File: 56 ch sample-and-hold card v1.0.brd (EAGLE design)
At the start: 170.8 x 36.2 mm, 124 parts, among them IC1 4051D, IC10 TL074JT, IC11 4051D, IC12 TL074JT, IC13 TL074JT, IC14 4051D, IC15 TL074JT, IC16 TL074JT, IC17 4051D, IC18 TL074JT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

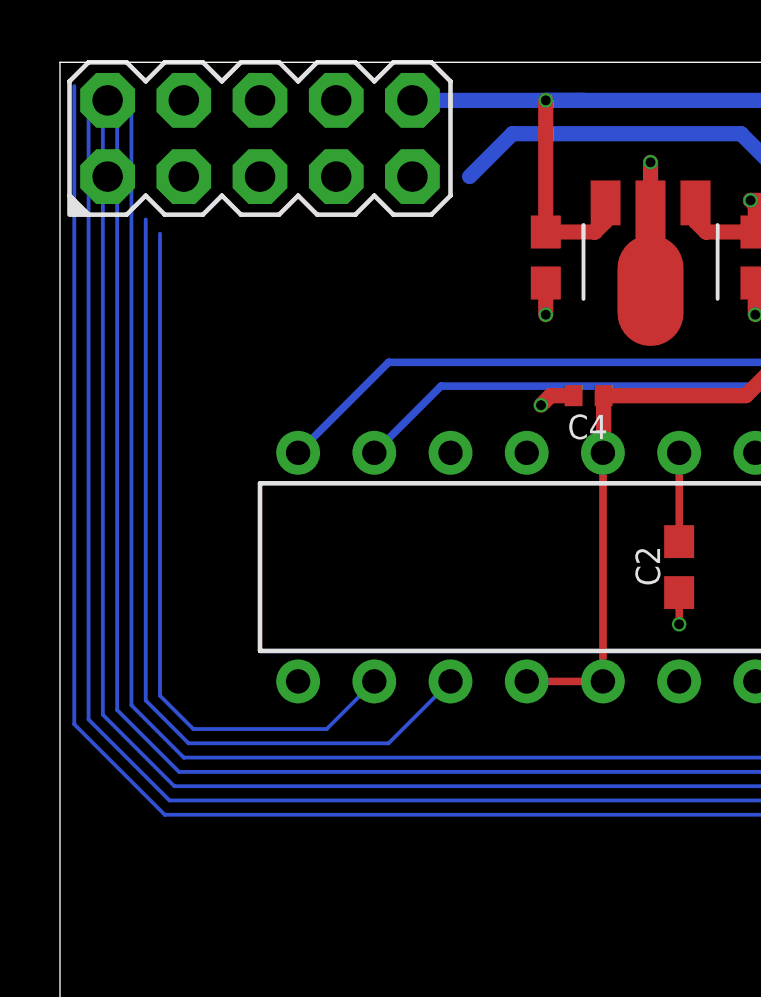
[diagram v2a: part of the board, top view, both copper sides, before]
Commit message: All routed, nothing tested
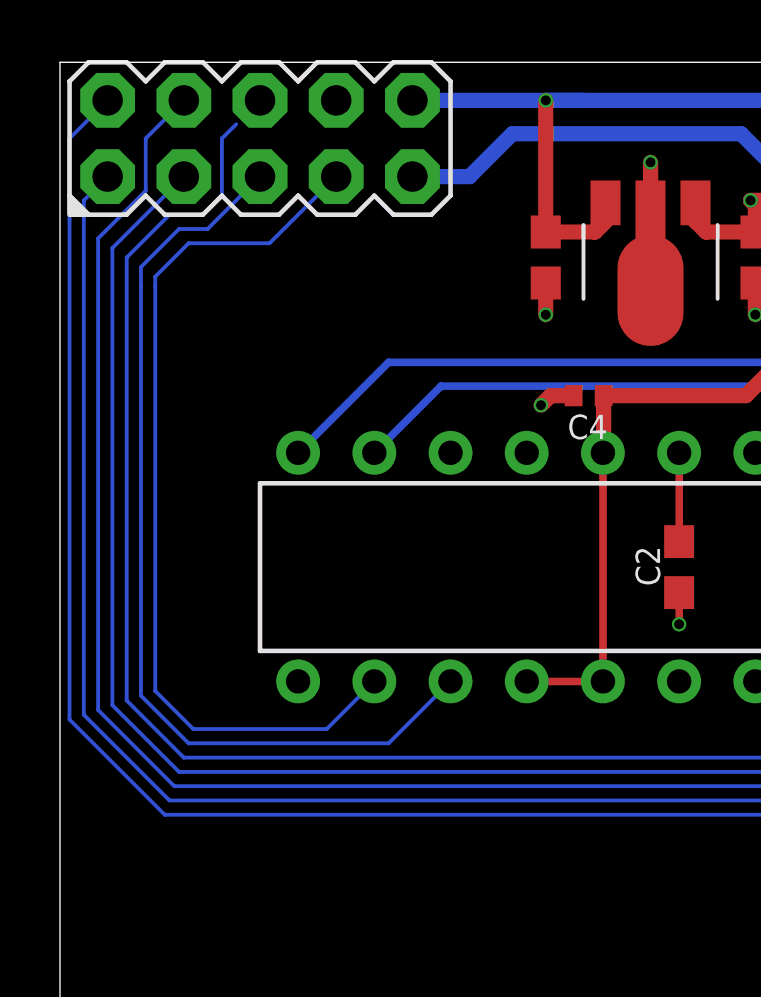
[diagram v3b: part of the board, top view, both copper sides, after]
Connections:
- new net GND: X1.8
- net +12V: now also X1.10
- net -12V: now also X1.9
- net A0: now also X1.2
- net A1: now also X1.1
- net A2: now also X1.4
- net INH_1: now also X1.3
- net INH_2: now also X1.6
- net SCK: now also X1.7
- net SDA: now also X1.5
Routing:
- net SCK: track 23.7 -> 29.7 mm
- net SDA: track 27.6 -> 31.3 mm
- net A1: track 202.0 -> 199.5 mm
- net -12V: track 191.3 -> 193.2 mm
- net INH_1: track 212.7 -> 210.9 mm
- net INH_2: track 177.0 -> 178.1 mm
- net +12V: track 196.6 -> 197.5 mm
- net A2: track 197.7 -> 198.6 mm
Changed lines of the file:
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@@
 <wire x1="23.495" y1="34.925" x2="17.4625" y2="34.925" width="0.508" layer="16"/>
 <wire x1="17.4625" y1="34.925" x2="16.1925" y2="34.925" width="0.508" layer="16"/>
-<wire x1="16.1925" y1="34.925" x2="12.7" y2="34.925" width="0.508" layer="16"/>
 <wire x1="16.1925" y1="30.53625" x2="17.83625" y2="30.53625" width="0.508" layer="1"/>
 <wire x1="18.186" y1="30.886" x2="18.186" y2="31.5085" width="0.508" layer="1"/>
@@
 <wire x1="77.94625" y1="29.36875" x2="67.78625" y2="29.36875" width="0.508" layer="16"/>
 <wire x1="57.62625" y1="29.36875" x2="47.46625" y2="29.36875" width="0.508" layer="16"/>
+<contactref element="X1" pad="10"/>
+<wire x1="16.1925" y1="34.925" x2="11.7475" y2="34.925" width="0.508" layer="16"/>
 </signal>
 <signal name="-12V">
@@
 <wire x1="59.69" y1="28.2575" x2="70.00875" y2="28.2575" width="0.508" layer="16"/>
 <wire x1="39.37" y1="28.2575" x2="49.68875" y2="28.2575" width="0.508" layer="16"/>
+<contactref element="X1" pad="9"/>
+<wire x1="13.6525" y1="32.385" x2="11.7475" y2="32.385" width="0.508" layer="16"/>
 </signal>
 <signal name="OUT_7">
@@
 <wire x1="36.5125" y1="11.1125" x2="28.2575" y2="11.1125" width="0.127" layer="16"/>
 <wire x1="117.7925" y1="14.7066" x2="117.7925" y2="11.1125" width="0.127" layer="1"/>
-<wire x1="3.4925" y1="11.1125" x2="0.47625" y2="14.12875" width="0.127" layer="16"/>
-<wire x1="0.47625" y1="14.12875" x2="0.47625" y2="35.40125" width="0.127" layer="16"/>
+<wire x1="3.4925" y1="11.1125" x2="0.3175" y2="14.2875" width="0.127" layer="16"/>
 <wire x1="28.2575" y1="11.1125" x2="3.4925" y2="11.1125" width="0.127" layer="16"/>
+<wire x1="0.3175" y1="30.95625" x2="0.3175" y2="33.655" width="0.127" layer="16"/>
+<wire x1="0.3175" y1="14.2875" x2="0.3175" y2="30.95625" width="0.127" layer="16"/>
+<contactref element="X1" pad="2"/>
+<wire x1="0.3175" y1="33.655" x2="1.5875" y2="34.925" width="0.127" layer="16"/>
 </signal>
 <signal name="A1">
@@
 <wire x1="35.2425" y1="11.58875" x2="28.09875" y2="11.58875" width="0.127" layer="16"/>
 <wire x1="116.5225" y1="14.7066" x2="116.5225" y2="11.58875" width="0.127" layer="1"/>
-<wire x1="3.65125" y1="11.58875" x2="0.9525" y2="14.2875" width="0.127" layer="16"/>
+<wire x1="3.65125" y1="11.58875" x2="0.79375" y2="14.44625" width="0.127" layer="16"/>
 <wire x1="28.09875" y1="11.58875" x2="3.65125" y2="11.58875" width="0.127" layer="16"/>
-<wire x1="0.9525" y1="14.2875" x2="0.9525" y2="35.2425" width="0.127" layer="16"/>
+<wire x1="0.79375" y1="31.59125" x2="0.79375" y2="14.44625" width="0.127" layer="16"/>
+<contactref element="X1" pad="1"/>
+<wire x1="1.5875" y1="32.385" x2="0.79375" y2="31.59125" width="0.127" layer="16"/>
 </signal>
 <signal name="A2">
@@
 <wire x1="33.9725" y1="12.065" x2="27.94" y2="12.065" width="0.127" layer="16"/>
 <wire x1="115.2525" y1="14.7066" x2="115.2525" y2="13.17625" width="0.127" layer="1"/>
-<wire x1="3.81" y1="12.065" x2="1.42875" y2="14.44625" width="0.127" layer="16"/>
-<wire x1="1.42875" y1="14.44625" x2="1.42875" y2="35.2425" width="0.127" layer="16"/>
+<wire x1="3.81" y1="12.065" x2="1.27" y2="14.605" width="0.127" layer="16"/>
 <wire x1="27.94" y1="12.065" x2="3.81" y2="12.065" width="0.127" layer="16"/>
+<wire x1="1.27" y1="14.605" x2="1.27" y2="30.32125" width="0.127" layer="16"/>
+<wire x1="1.27" y1="30.32125" x2="2.8575" y2="31.90875" width="0.127" layer="16"/>
+<wire x1="2.8575" y1="31.90875" x2="2.8575" y2="33.655" width="0.127" layer="16"/>
+<contactref element="X1" pad="4"/>
+<wire x1="2.8575" y1="33.655" x2="4.1275" y2="34.925" width="0.127" layer="16"/>
 </signal>
 <signal name="INH_1">
@@
 <wire x1="114.45875" y1="12.54125" x2="113.9825" y2="12.54125" width="0.127" layer="16"/>
 <wire x1="32.86125" y1="12.54125" x2="27.78125" y2="12.54125" width="0.127" layer="16"/>
-<wire x1="3.96875" y1="12.54125" x2="1.905" y2="14.605" width="0.127" layer="16"/>
-<wire x1="1.905" y1="14.605" x2="1.905" y2="35.2425" width="0.127" layer="16"/>
+<wire x1="3.96875" y1="12.54125" x2="1.74625" y2="14.76375" width="0.127" layer="16"/>
+<wire x1="1.74625" y1="14.76375" x2="1.74625" y2="30.00375" width="0.127" layer="16"/>
 <wire x1="27.78125" y1="12.54125" x2="3.96875" y2="12.54125" width="0.127" layer="16"/>
+<contactref element="X1" pad="3"/>
+<wire x1="1.74625" y1="30.00375" x2="4.1275" y2="32.385" width="0.127" layer="16"/>
 </signal>
 <signal name="DAC_1">
@@
 <wire x1="56.8325" y1="13.0175" x2="56.8325" y2="19.3675" width="0.127" layer="16"/>
 <wire x1="97.4725" y1="17.78" x2="97.4725" y2="13.0175" width="0.127" layer="16"/>
-<wire x1="4.1275" y1="13.0175" x2="2.38125" y2="14.76375" width="0.127" layer="16"/>
-<wire x1="2.38125" y1="14.76375" x2="2.38125" y2="35.2425" width="0.127" layer="16"/>
+<wire x1="4.1275" y1="13.0175" x2="2.2225" y2="14.9225" width="0.127" layer="16"/>
+<wire x1="2.2225" y1="14.9225" x2="2.2225" y2="29.68625" width="0.127" layer="16"/>
 <wire x1="27.6225" y1="13.0175" x2="4.1275" y2="13.0175" width="0.127" layer="16"/>
+<wire x1="3.65125" y1="31.115" x2="4.7625" y2="31.115" width="0.127" layer="16"/>
+<wire x1="4.7625" y1="31.115" x2="5.3975" y2="31.75" width="0.127" layer="16"/>
+<wire x1="5.3975" y1="33.655" x2="5.87375" y2="34.13125" width="0.127" layer="16"/>
+<wire x1="2.2225" y1="29.68625" x2="3.65125" y2="31.115" width="0.127" layer="16"/>
+<wire x1="5.3975" y1="31.75" x2="5.3975" y2="33.655" width="0.127" layer="16"/>
+<contactref element="X1" pad="6"/>
+<wire x1="5.87375" y1="34.13125" x2="6.6675" y2="34.925" width="0" layer="19" extent="16-16"/>
 </signal>
 <signal name="DAC_2">
@@
 <contactref element="IC2" pad="10"/>
 <wire x1="10.4775" y1="15.5575" x2="8.89" y2="13.97" width="0.127" layer="16"/>
-<wire x1="4.445" y1="13.97" x2="3.33375" y2="15.08125" width="0.127" layer="16"/>
+<wire x1="4.445" y1="13.97" x2="3.175" y2="15.24" width="0.127" layer="16"/>
 <wire x1="8.89" y1="13.97" x2="4.445" y2="13.97" width="0.127" layer="16"/>
-<wire x1="3.33375" y1="15.08125" x2="3.33375" y2="30.48" width="0.127" layer="16"/>
+<wire x1="3.175" y1="15.24" x2="3.175" y2="28.73375" width="0.127" layer="16"/>
+<wire x1="3.175" y1="28.73375" x2="3.175" y2="29.05125" width="0.127" layer="16"/>
+<wire x1="3.175" y1="29.05125" x2="4.28625" y2="30.1625" width="0.127" layer="16"/>
+<wire x1="4.28625" y1="30.1625" x2="6.985" y2="30.1625" width="0.127" layer="16"/>
+<contactref element="X1" pad="7"/>
+<wire x1="6.985" y1="30.1625" x2="9.2075" y2="32.385" width="0.127" layer="16"/>
 </signal>
 <signal name="SDA">
 <contactref element="IC2" pad="11"/>
 <wire x1="13.0175" y1="15.5575" x2="10.95375" y2="13.49375" width="0.127" layer="16"/>
-<wire x1="4.28625" y1="13.49375" x2="2.8575" y2="14.9225" width="0.127" layer="16"/>
+<wire x1="4.28625" y1="13.49375" x2="2.69875" y2="15.08125" width="0.127" layer="16"/>
 <wire x1="10.95375" y1="13.49375" x2="4.28625" y2="13.49375" width="0.127" layer="16"/>
-<wire x1="2.8575" y1="14.9225" x2="2.8575" y2="30.95625" width="0.127" layer="16"/>
+<wire x1="2.69875" y1="28.73375" x2="2.69875" y2="15.08125" width="0.127" layer="16"/>
+<wire x1="2.69875" y1="28.73375" x2="2.69875" y2="29.36875" width="0.127" layer="16"/>
+<wire x1="2.69875" y1="29.36875" x2="3.96875" y2="30.63875" width="0.127" layer="16"/>
+<wire x1="3.96875" y1="30.63875" x2="4.92125" y2="30.63875" width="0.127" layer="16"/>
+<contactref element="X1" pad="5"/>
+<wire x1="4.92125" y1="30.63875" x2="6.6675" y2="32.385" width="0.127" layer="16"/>
 </signal>
 <signal name="N$8">
@@
 <wire x1="20.6375" y1="20.2175" x2="20.6375" y2="23.1775" width="0.254" layer="1"/>
 </signal>
+<signal name="GND">
+<contactref element="X1" pad="8"/>
+</signal>
 </signals>

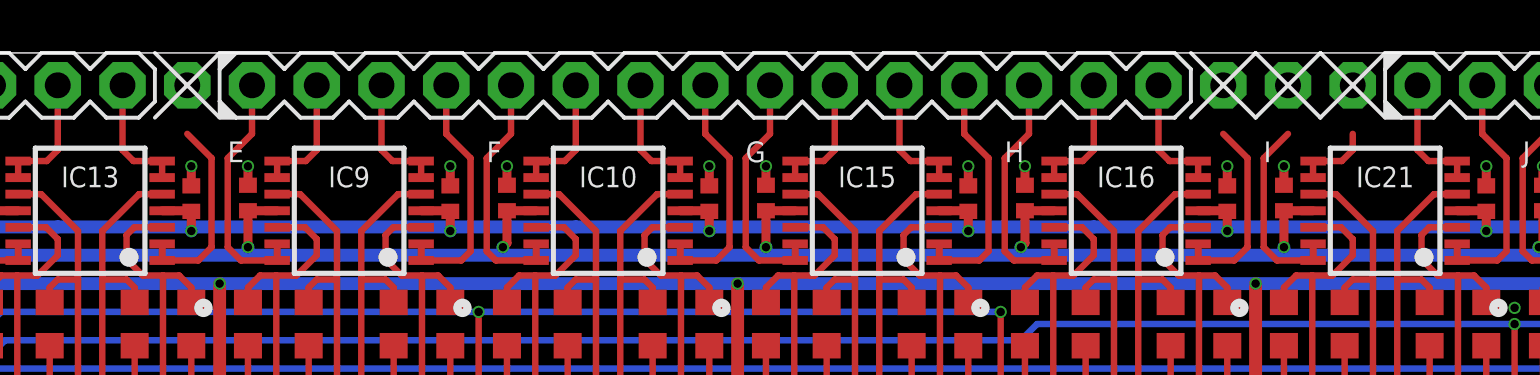
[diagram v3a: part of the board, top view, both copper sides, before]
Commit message: Moved spare connectors to prevent misplacement of headers
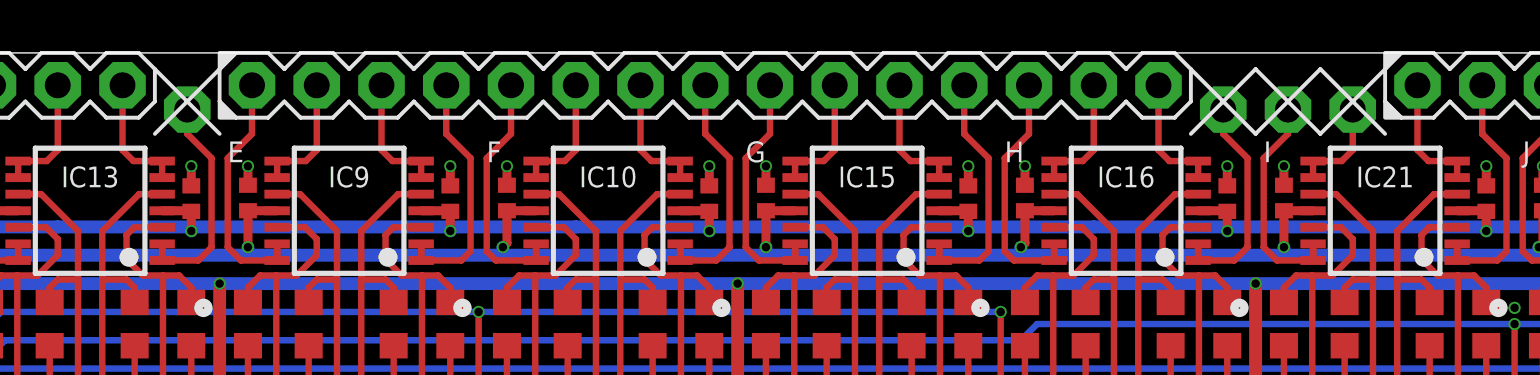
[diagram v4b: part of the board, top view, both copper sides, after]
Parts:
- moved X5 0.95 mm to (67.6, 34.0)
- moved X6 0.95 mm to (110.8, 34.0)
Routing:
- net OUT_33: track 3.02 -> 3.97 mm
- net OUT_32: track 8.34 -> 9.29 mm
- net OUT_31: track 8.34 -> 9.29 mm
- net OUT_15: track 8.34 -> 9.29 mm
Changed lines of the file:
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@@
 <text x="150.495" y="31.90875" size="0.8128" layer="25" font="vector">M</text>
 <text x="160.655" y="31.90875" size="0.8128" layer="25" font="vector">N</text>
-<wire x1="66.3575" y1="36.195" x2="68.8975" y2="33.655" width="0.1524" layer="25"/>
-<wire x1="68.8975" y1="36.195" x2="66.3575" y2="33.655" width="0.1524" layer="25"/>
-<wire x1="106.9975" y1="36.195" x2="109.5375" y2="33.655" width="0.1524" layer="25"/>
-<wire x1="109.5375" y1="36.195" x2="106.9975" y2="33.655" width="0.1524" layer="25"/>
-<wire x1="109.5375" y1="36.195" x2="112.0775" y2="33.655" width="0.1524" layer="25"/>
-<wire x1="109.5375" y1="33.655" x2="112.0775" y2="36.195" width="0.1524" layer="25"/>
-<wire x1="112.0775" y1="36.195" x2="114.6175" y2="33.655" width="0.1524" layer="25"/>
-<wire x1="112.0775" y1="33.655" x2="114.6175" y2="36.195" width="0.1524" layer="25"/>
+<wire x1="66.3575" y1="35.56" x2="68.8975" y2="33.02" width="0.1524" layer="25"/>
+<wire x1="68.8975" y1="35.56" x2="66.3575" y2="33.02" width="0.1524" layer="25"/>
+<wire x1="106.9975" y1="35.56" x2="109.5375" y2="33.02" width="0.1524" layer="25"/>
+<wire x1="109.5375" y1="35.56" x2="106.9975" y2="33.02" width="0.1524" layer="25"/>
+<wire x1="109.5375" y1="35.56" x2="112.0775" y2="33.02" width="0.1524" layer="25"/>
+<wire x1="109.5375" y1="33.02" x2="112.0775" y2="35.56" width="0.1524" layer="25"/>
+<wire x1="112.0775" y1="35.56" x2="114.6175" y2="33.02" width="0.1524" layer="25"/>
+<wire x1="112.0775" y1="33.02" x2="114.6175" y2="35.56" width="0.1524" layer="25"/>
 <wire x1="15.24" y1="33.655" x2="29.4894" y2="33.655" width="0.127" layer="51"/>
 </plain>
@@
 <attribute name="VALUE" x="167.9575" y="32.004" size="1.27" layer="27" ratio="10"/>
 </element>
-<element name="X5" library="joakim" package="MA01N-1J" value="DNM" x="67.6275" y="34.925" smashed="yes">
-<attribute name="VALUE" x="65.0875" y="32.004" size="1.27" layer="27" ratio="10"/>
-</element>
-<element name="X6" library="joakim" package="MA03N-1J" value="DNM" x="110.8075" y="34.925" smashed="yes">
-<attribute name="VALUE" x="106.9975" y="32.004" size="1.27" layer="27" ratio="10"/>
+<element name="X5" library="joakim" package="MA01N-1J" value="DNM" x="67.6275" y="33.9725" smashed="yes">
+<attribute name="VALUE" x="65.0875" y="31.0515" size="1.27" layer="27" ratio="10"/>
+</element>
+<element name="X6" library="joakim" package="MA03N-1J" value="DNM" x="110.8075" y="33.9725" smashed="yes">
+<attribute name="VALUE" x="106.9975" y="31.0515" size="1.27" layer="27" ratio="10"/>
 </element>
 </elements>
@@
 <wire x1="68.05875" y1="28.05375" x2="68.58" y2="28.575" width="0.254" layer="1"/>
 <wire x1="68.58" y1="28.575" x2="68.58" y2="32.0675" width="0.254" layer="1"/>
-<wire x1="68.58" y1="32.0675" x2="67.6275" y2="33.02" width="0.254" layer="1"/>
+<wire x1="67.6275" y1="33.02" x2="68.58" y2="32.0675" width="0.254" layer="1"/>
 <contactref element="X5" pad="1"/>
-<wire x1="67.6275" y1="33.02" x2="67.6275" y2="34.925" width="0" layer="19" extent="1-1"/>
+<wire x1="67.6275" y1="33.9725" x2="67.6275" y2="33.02" width="0.254" layer="1"/>
 </signal>
 <signal name="+5V">
@@
 <wire x1="108.69875" y1="28.05375" x2="109.22" y2="28.575" width="0.254" layer="1"/>
 <wire x1="109.22" y1="28.575" x2="109.22" y2="32.0675" width="0.254" layer="1"/>
-<wire x1="109.22" y1="32.0675" x2="108.2675" y2="33.02" width="0.254" layer="1"/>
+<wire x1="108.2675" y1="33.02" x2="109.22" y2="32.0675" width="0.254" layer="1"/>
 <contactref element="X6" pad="1"/>
-<wire x1="108.2675" y1="33.02" x2="108.2675" y2="34.925" width="0" layer="19" extent="1-1"/>
+<wire x1="108.2675" y1="33.9725" x2="108.2675" y2="33.02" width="0.254" layer="1"/>
 </signal>
 <signal name="OUT_30">
@@
 <wire x1="111.8375" y1="28.73375" x2="111.7925" y2="28.68875" width="0.254" layer="1"/>
 <wire x1="111.7925" y1="28.05375" x2="110.37625" y2="28.05375" width="0.254" layer="1"/>
-<wire x1="109.855" y1="32.0675" x2="110.8075" y2="33.02" width="0.254" layer="1"/>
+<wire x1="110.8075" y1="33.02" x2="109.855" y2="32.0675" width="0.254" layer="1"/>
 <wire x1="110.37625" y1="28.05375" x2="109.855" y2="28.575" width="0.254" layer="1"/>
 <wire x1="109.855" y1="28.575" x2="109.855" y2="32.0675" width="0.254" layer="1"/>
 <contactref element="X6" pad="2"/>
-<wire x1="110.8075" y1="33.02" x2="110.8075" y2="34.925" width="0" layer="19" extent="1-1"/>
+<wire x1="110.8075" y1="33.9725" x2="110.8075" y2="33.02" width="0.254" layer="1"/>
 </signal>
 <signal name="OUT_34">
@@
 <wire x1="111.7925" y1="31.30375" x2="111.7925" y2="31.95375" width="0.254" layer="1"/>
 <wire x1="111.7925" y1="31.95375" x2="112.91625" y2="31.95375" width="0.254" layer="1"/>
-<wire x1="112.91625" y1="31.95375" x2="113.3475" y2="32.385" width="0.254" layer="1"/>
-<wire x1="113.3475" y1="32.385" x2="113.3475" y2="33.02" width="0.254" layer="1"/>
+<wire x1="113.3475" y1="32.385" x2="112.91625" y2="31.95375" width="0.254" layer="1"/>
 <contactref element="X6" pad="3"/>
-<wire x1="113.3475" y1="33.02" x2="113.3475" y2="34.925" width="0" layer="19" extent="1-1"/>
+<wire x1="113.3475" y1="33.9725" x2="113.3475" y2="32.385" width="0.254" layer="1"/>
 </signal>
 <signal name="IN_36">

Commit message: Added silk
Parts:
- added U$1: (no value), joakim:XONIK_LOGO_60
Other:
- board text added: "+V"
- board text added: "-V"
- board text added: "0"
- board text added: "1"
- board text added: "2"
- board text added: "3"
- board text added: "4"
- board text added: "4VOB"
- board text added: "5"
- board text added: "56 channel CV generator"
- board text added: "6"
- board text added: "7"
- board text added: "8"
- board text added: "9"
- board text added: "A0"
- board text added: "A1"
- board text added: "A2"
- board text added: "GND"
- board text added: "IH1"
- board text added: "IH2"
- board text added: "SCK"
- board text added: "SDA"

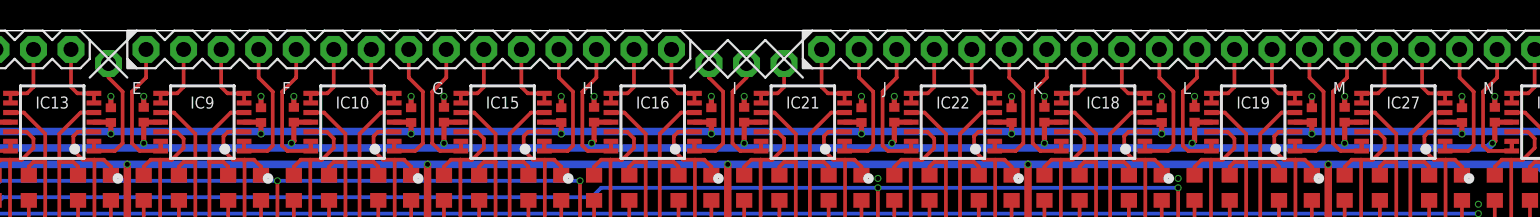
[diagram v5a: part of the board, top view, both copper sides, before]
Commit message: Split 22p into 15p and 7p
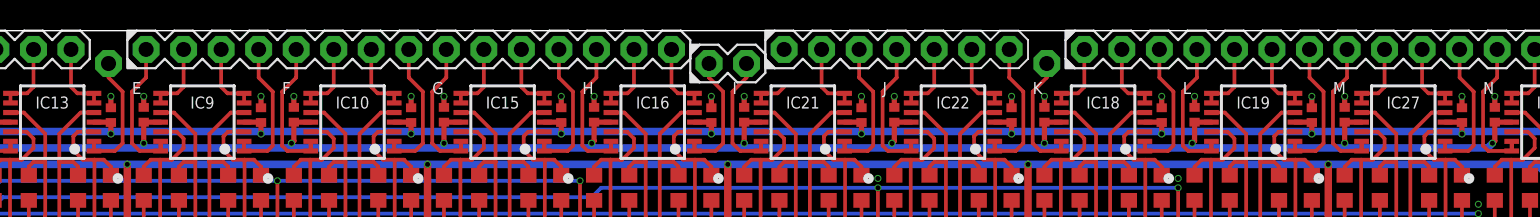
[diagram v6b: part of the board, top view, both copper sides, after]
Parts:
- removed X6: DNM, joakim:MA03N-1J
- added X7: FEMALE, joakim:MA15-1J
- added X8: FEMALE, joakim:MA07-1J
- added X9: DNM, joakim:MA02-1J
- IC1, IC11, IC14, IC17, IC20, IC26, IC7: value 4051D -> 74HCT4051D
- X4: value FEMALE -> DNM; device joakim:MA22-1J -> joakim:MA01N-1J
- moved X4 12.7 mm to (131.1, 34.0)
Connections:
- net OUT_31: now also X9.1; no longer X6.1
- net OUT_32: now also X9.2; no longer X6.2
- net OUT_33: now also X8.1; no longer X6.3
- net OUT_34: now also X8.2; no longer X4.1
- net OUT_35: now also X8.3; no longer X4.2
- net OUT_36: now also X8.4; no longer X4.3
- net OUT_37: now also X8.5; no longer X4.4
- net OUT_38: now also X8.6; no longer X4.5
- net OUT_39: now also X8.7; no longer X4.6
- net OUT_40: now also X4.1; no longer X4.7
- net OUT_41: now also X7.1; no longer X4.8
- net OUT_42: now also X7.2; no longer X4.9
- net OUT_43: now also X7.3; no longer X4.10
- net OUT_44: now also X7.4; no longer X4.11
- net OUT_45: now also X7.5; no longer X4.12
- net OUT_46: now also X7.6; no longer X4.13
- net OUT_47: now also X7.7; no longer X4.14
- net OUT_48: now also X7.8; no longer X4.15
- net OUT_49: now also X7.9; no longer X4.16
- net OUT_50: now also X7.10; no longer X4.17
- net OUT_51: now also X7.11; no longer X4.18
- net OUT_52: now also X7.12; no longer X4.19
- net OUT_53: now also X7.13; no longer X4.20
- net OUT_54: now also X7.14; no longer X4.21
- net OUT_55: now also X7.15; no longer X4.22
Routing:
- net OUT_33: track 3.97 -> 2.38 mm
- net OUT_40: track 10.2 -> 9.29 mm
